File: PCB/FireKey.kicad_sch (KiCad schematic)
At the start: 76 parts, among them SW1 SW_MEC_5E, U1 Arduino_Pro_Micro_USB-C

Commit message: worked on schematic structure
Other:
- note added: "Central MCU"
- note added: "Key Matrix"
- note added: "LED Decoupling"
- note added: "LED Strip"
- note added: "OLED Display"
- note added: "PCB Mounting"
- note added: "RESET Button"
- moved on the sheet: C1, C10, C11, C12, C13, C14, C15, C2, C3, C4, C5, C6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

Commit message: Worked on BOM
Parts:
- H1, H10, H11, H12, H2, H3, H4, H5, H6, H7, H8, H9: Part# (none) -> -; Supplier (none) -> -
- KEY1, KEY10, KEY11, KEY12, KEY13, KEY14, KEY15, KEY2, KEY3, KEY4, KEY5, KEY6, KEY7, KEY8, KEY9: Supplier (none) -> AliExpress
- OLED1: Part# (none) -> -; Supplier (none) -> AliExpress
- U1: Part# (none) -> -; Pinout https://golem.hu/pic/pro_micro_pinout.jpg -> (none); Supplier (none) -> AliExpress

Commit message: start adding custom footprints
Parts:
- SW1: footprint (none) -> Button_Switch_SMD:SW_SPST_TL3342
- U1: footprint (none) -> Custom_MCU:Arduino_Pro_Micro_USB-C
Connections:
- net GND: now also U1.90 (GND), U1.91 (GND), U1.93 (GND); no longer U1. (VCC)
- net RST: now also U1.94 (RST); no longer U1. (VCC)
- net VCC: now also U1.92 (RAW); no longer U1. (VCC)
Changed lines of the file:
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@@
   (junction (at 266.7 87.63) (diameter 0) (color 0 0 0 0)
   )
-  (no_connect (at 93.98 154.94))
-  (no_connect (at 93.98 147.32))
-  (no_connect (at 93.98 142.24))
-  (no_connect (at 93.98 149.86))
-  (no_connect (at 76.2 137.16))
-  (no_connect (at 93.98 152.4))
-  (no_connect (at 76.2 149.86))
+  (no_connect (at 95.25 154.94))
+  (no_connect (at 95.25 147.32))
+  (no_connect (at 95.25 142.24))
+  (no_connect (at 95.25 149.86))
+  (no_connect (at 74.93 137.16))
+  (no_connect (at 95.25 152.4))
+  (no_connect (at 74.93 149.86))
   (no_connect (at 229.87 111.76))
-  (no_connect (at 76.2 134.62))
+  (no_connect (at 74.93 134.62))
   (wire (pts (xy 170.18 83.82) (xy 176.53 83.82))
     (stroke (width 0) (type default) (color 0 0 0 0))
@@
     (stroke (width 0) (type default) (color 0 0 0 0))
   )
+  (wire (pts (xy 74.93 134.62) (xy 76.2 134.62))
+    (stroke (width 0) (type default) (color 0 0 0 0))
+  )
   (wire (pts (xy 231.14 30.48) (xy 229.87 30.48))
     (stroke (width 0) (type default) (color 0 0 0 0))
@@
     (stroke (width 0) (type default) (color 0 0 0 0))
   )
+  (wire (pts (xy 95.25 149.86) (xy 93.98 149.86))
+    (stroke (width 0) (type default) (color 0 0 0 0))
+  )
   (wire (pts (xy 270.51 151.13) (xy 270.51 149.86))
     (stroke (width 0) (type default) (color 0 0 0 0))
@@
     (stroke (width 0) (type default) (color 0 0 0 0))
   )
+  (wire (pts (xy 74.93 149.86) (xy 76.2 149.86))
+    (stroke (width 0) (type default) (color 0 0 0 0))
+  )
   (wire (pts (xy 48.26 91.44) (xy 48.26 101.6))
     (stroke (width 0) (type default) (color 0 0 0 0))
@@
     (stroke (width 0) (type default) (color 0 0 0 0))
   )
+  (wire (pts (xy 74.93 137.16) (xy 76.2 137.16))
+    (stroke (width 0) (type default) (color 0 0 0 0))
+  )
   (polyline (pts (xy 284.48 124.46) (xy 242.57 124.46))
     (stroke (width 0) (type default) (color 0 0 0 0))
@@
     (stroke (width 0) (type default) (color 0 0 0 0))
   )
+  (wire (pts (xy 95.25 152.4) (xy 93.98 152.4))
+    (stroke (width 0) (type default) (color 0 0 0 0))
+  )
   (wire (pts (xy 176.53 83.82) (xy 199.39 83.82))
     (stroke (width 0) (type default) (color 0 0 0 0))
@@
     (stroke (width 0) (type default) (color 0 0 0 0))
   )
+  (wire (pts (xy 95.25 142.24) (xy 93.98 142.24))
+    (stroke (width 0) (type default) (color 0 0 0 0))
+  )
   (wire (pts (xy 64.77 60.96) (xy 64.77 76.2))
     (stroke (width 0) (type default) (color 0 0 0 0))
@@
     (stroke (width 0) (type default) (color 0 0 0 0))
   )
+  (wire (pts (xy 95.25 147.32) (xy 93.98 147.32))
+    (stroke (width 0) (type default) (color 0 0 0 0))
+  )
   (wire (pts (xy 53.34 30.48) (xy 54.61 30.48))
     (stroke (width 0) (type default) (color 0 0 0 0))
@@
     (stroke (width 0) (type default) (color 0 0 0 0))
   )
+  (wire (pts (xy 95.25 154.94) (xy 93.98 154.94))
+    (stroke (width 0) (type default) (color 0 0 0 0))
+  )
   (wire (pts (xy 162.56 50.8) (xy 168.91 50.8))
     (stroke (width 0) (type default) (color 0 0 0 0))
@@
     (property "Reference" "U1" (id 0) (at 85.09 127 0))
     (property "Value" "Arduino_Pro_Micro_USB-C" (id 1) (at 85.09 129.54 0))
-    (property "Footprint" "" (id 2) (at 83.82 129.54 0)
+    (property "Footprint" "Custom_MCU:Arduino_Pro_Micro_USB-C" (id 2) (at 83.82 129.54 0)
       (effects (font (size 1.27 1.27)) hide)
     )
@@
       (effects (font (size 1.27 1.27)) hide)
     )
-    (pin "")
-    (pin "")
-    (pin "")
-    (pin "")
-    (pin "")
-    (pin "")
     (pin "0")
     (pin "1")
@@
     (pin "8")
     (pin "9")
+    (pin "90")
+    (pin "91")
+    (pin "92")
+    (pin "93")
+    (pin "94")
+    (pin "95")
   )
   (symbol (lib_id "Device:D") (at 36.83 80.01 90) (unit 1)
@@
     (pin "1")
   )
-  (symbol (lib_name "DY-S352818{slash}6812-2T_8") (lib_id "Custom_Parts:DY-S352818{slash}6812-2T") (at 176.53 71.12 0) (unit 1)
+  (symbol (lib_id "Custom_Parts:DY-S352818{slash}6812-2T") (at 176.53 71.12 0) (unit 1)
     (in_bom yes) (on_board yes)
     (property "Reference" "LED7" (id 0) (at 177.8 64.77 0)
@@
   (symbol (lib_id "Custom_Modules:OLED_1.3_4P") (at 119.38 41.91 0) (unit 1)
     (in_bom yes) (on_board yes)
-    (property "Reference" "OLED1" (id 0) (at 119.38 49.53 0))
+    (property "Reference" "OLED1" (id 0) (at 119.38 50.8 0))
     (property "Value" "OLED_1.3_4P" (id 1) (at 119.38 45.72 0))
     (property "Footprint" "" (id 2) (at 119.38 27.94 0)
@@
     (pin "1")
   )
-  (symbol (lib_name "DY-S352818{slash}6812-2T_10") (lib_id "Custom_Parts:DY-S352818{slash}6812-2T") (at 176.53 30.48 0) (unit 1)
+  (symbol (lib_id "Custom_Parts:DY-S352818{slash}6812-2T") (at 176.53 30.48 0) (unit 1)
     (in_bom yes) (on_board yes)
     (property "Reference" "LED1" (id 0) (at 177.8 24.13 0)
@@
     (pin "1")
   )
-  (symbol (lib_name "DY-S352818{slash}6812-2T_7") (lib_id "Custom_Parts:DY-S352818{slash}6812-2T") (at 199.39 111.76 0) (unit 1)
+  (symbol (lib_id "Custom_Parts:DY-S352818{slash}6812-2T") (at 199.39 111.76 0) (unit 1)
     (in_bom yes) (on_board yes)
     (property "Reference" "LED14" (id 0) (at 200.66 105.41 0)
@@
     (pin "2")
   )
-  (symbol (lib_name "DY-S352818{slash}6812-2T_9") (lib_id "Custom_Parts:DY-S352818{slash}6812-2T") (at 176.53 50.8 0) (unit 1)
+  (symbol (lib_id "Custom_Parts:DY-S352818{slash}6812-2T") (at 176.53 50.8 0) (unit 1)
     (in_bom yes) (on_board yes)
     (property "Reference" "LED4" (id 0) (at 177.8 44.45 0)
@@
     (pin "4")
   )
-  (symbol (lib_name "DY-S352818{slash}6812-2T_1") (lib_id "Custom_Parts:DY-S352818{slash}6812-2T") (at 222.25 30.48 0) (unit 1)
+  (symbol (lib_id "Custom_Parts:DY-S352818{slash}6812-2T") (at 222.25 30.48 0) (unit 1)
     (in_bom yes) (on_board yes)
     (property "Reference" "LED3" (id 0) (at 223.52 24.13 0)
@@
     (pin "1")
   )
-  (symbol (lib_name "DY-S352818{slash}6812-2T_14") (lib_id "Custom_Parts:DY-S352818{slash}6812-2T") (at 199.39 50.8 0) (unit 1)
+  (symbol (lib_id "Custom_Parts:DY-S352818{slash}6812-2T") (at 199.39 50.8 0) (unit 1)
     (in_bom yes) (on_board yes)
     (property "Reference" "LED5" (id 0) (at 200.66 44.45 0)
@@
     (pin "2")
   )
-  (symbol (lib_name "DY-S352818{slash}6812-2T_11") (lib_id "Custom_Parts:DY-S352818{slash}6812-2T") (at 199.39 71.12 0) (unit 1)
+  (symbol (lib_id "Custom_Parts:DY-S352818{slash}6812-2T") (at 199.39 71.12 0) (unit 1)
     (in_bom yes) (on_board yes)
     (property "Reference" "LED8" (id 0) (at 200.66 64.77 0)
@@
     (pin "4")
   )
-  (symbol (lib_name "DY-S352818{slash}6812-2T_12") (lib_id "Custom_Parts:DY-S352818{slash}6812-2T") (at 199.39 91.44 0) (unit 1)
+  (symbol (lib_id "Custom_Parts:DY-S352818{slash}6812-2T") (at 199.39 91.44 0) (unit 1)
     (in_bom yes) (on_board yes)
     (property "Reference" "LED11" (id 0) (at 200.66 85.09 0)
@@
     (pin "4")
   )
-  (symbol (lib_name "DY-S352818{slash}6812-2T_4") (lib_id "Custom_Parts:DY-S352818{slash}6812-2T") (at 222.25 50.8 0) (unit 1)
+  (symbol (lib_id "Custom_Parts:DY-S352818{slash}6812-2T") (at 222.25 50.8 0) (unit 1)
     (in_bom yes) (on_board yes)
     (property "Reference" "LED6" (id 0) (at 223.52 44.45 0)
@@
     (pin "1")
   )
-  (symbol (lib_name "DY-S352818{slash}6812-2T_6") (lib_id "Custom_Parts:DY-S352818{slash}6812-2T") (at 176.53 111.76 0) (unit 1)
+  (symbol (lib_id "Custom_Parts:DY-S352818{slash}6812-2T") (at 176.53 111.76 0) (unit 1)
     (in_bom yes) (on_board yes)
     (property "Reference" "LED13" (id 0) (at 177.8 105.41 0)
@@
     (pin "4")
   )
-  (symbol (lib_name "DY-S352818{slash}6812-2T_2") (lib_id "Custom_Parts:DY-S352818{slash}6812-2T") (at 222.25 91.44 0) (unit 1)
+  (symbol (lib_id "Custom_Parts:DY-S352818{slash}6812-2T") (at 222.25 91.44 0) (unit 1)
     (in_bom yes) (on_board yes)
     (property "Reference" "LED12" (id 0) (at 223.52 85.09 0)
@@
     (pin "1")
   )
-  (symbol (lib_name "DY-S352818{slash}6812-2T_3") (lib_id "Custom_Parts:DY-S352818{slash}6812-2T") (at 222.25 111.76 0) (unit 1)
+  (symbol (lib_id "Custom_Parts:DY-S352818{slash}6812-2T") (at 222.25 111.76 0) (unit 1)
     (in_bom yes) (on_board yes)
     (property "Reference" "LED15" (id 0) (at 223.52 105.41 0)
@@
     (property "Reference" "SW1" (id 0) (at 264.16 140.97 0))
     (property "Value" "SW_MEC_5E" (id 1) (at 264.16 143.51 0))
-    (property "Footprint" "" (id 2) (at 264.16 143.51 0)
+    (property "Footprint" "Button_Switch_SMD:SW_SPST_TL3342" (id 2) (at 264.16 143.51 0)
       (effects (font (size 1.27 1.27)) hide)
     )
@@
     (pin "1")
   )
-  (symbol (lib_name "DY-S352818{slash}6812-2T_13") (lib_id "Custom_Parts:DY-S352818{slash}6812-2T") (at 199.39 30.48 0) (unit 1)
+  (symbol (lib_id "Custom_Parts:DY-S352818{slash}6812-2T") (at 199.39 30.48 0) (unit 1)
     (in_bom yes) (on_board yes)
     (property "Reference" "LED2" (id 0) (at 200.66 24.13 0)
@@
     (pin "2")
   )
-  (symbol (lib_name "DY-S352818{slash}6812-2T_5") (lib_id "Custom_Parts:DY-S352818{slash}6812-2T") (at 222.25 71.12 0) (unit 1)
+  (symbol (lib_id "Custom_Parts:DY-S352818{slash}6812-2T") (at 222.25 71.12 0) (unit 1)
     (in_bom yes) (on_board yes)
     (property "Reference" "LED9" (id 0) (at 223.52 64.77 0)
@@
     )
     (path "/c7b5504d-1a0d-40d4-ad19-3310d0f5f11d"
-      (reference "SW1") (unit 1) (value "SW_MEC_5E") (footprint "")
+      (reference "SW1") (unit 1) (value "SW_MEC_5E") (footprint "Button_Switch_SMD:SW_SPST_TL3342")
     )
     (path "/051f7d79-ef19-4f53-afce-cb909f526a33"
-      (reference "U1") (unit 1) (value "Arduino_Pro_Micro_USB-C") (footprint "")
+      (reference "U1") (unit 1) (value "Arduino_Pro_Micro_USB-C") (footprint "Custom_MCU:Arduino_Pro_Micro_USB-C")
     )
   )

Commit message: updated schematic
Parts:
- H1, H2, H3, H4: footprint (none) -> TestPoint:TestPoint_Pad_D2.5mm
- LED1, LED10, LED11, LED12, LED13, LED14, LED15, LED2, LED3, LED4, LED5, LED6, LED7, LED8, LED9: footprint (none) -> Custom_Parts:DY-S352818-6812-2T
- OLED1: footprint (none) -> Custom_Module:OLED_1.3_4P_withM2.5Holes

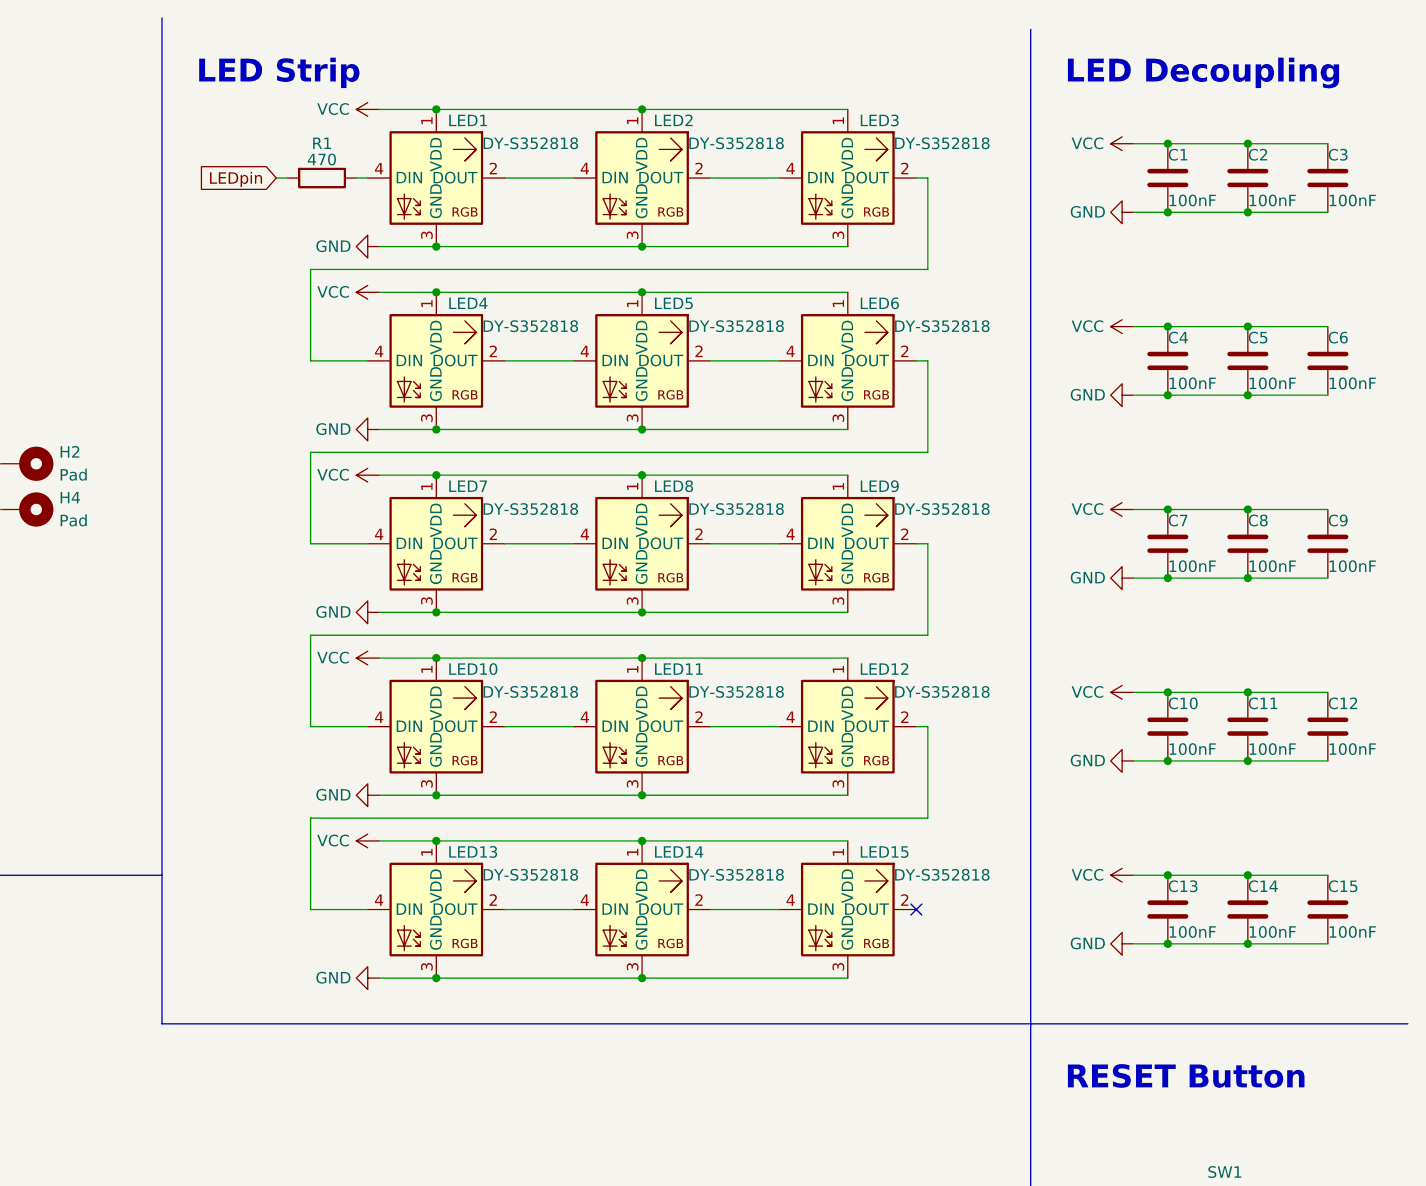
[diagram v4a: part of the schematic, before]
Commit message: simplified led strip tracing
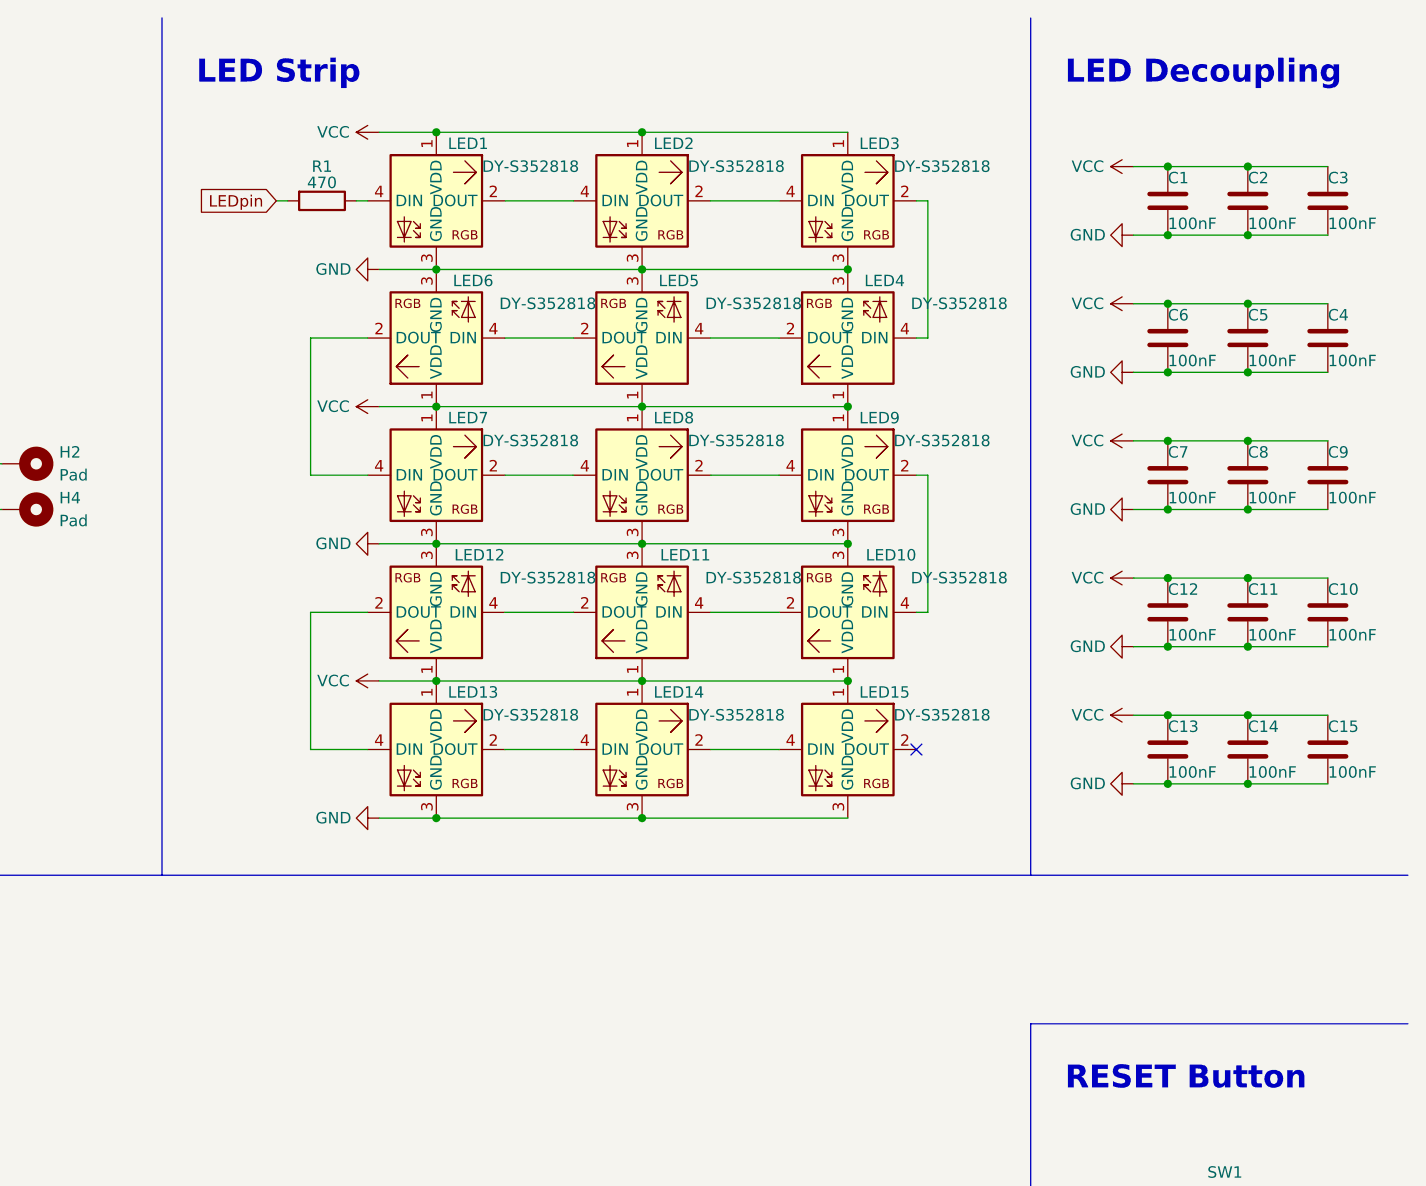
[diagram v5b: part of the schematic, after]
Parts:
- renumbered C12 to C10, C10 to C12, C6 to C4, C4 to C6
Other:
- moved on the sheet: C1, C10, C11, C12, C13, C14, C15, C2, C3, C4, C5, C6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
